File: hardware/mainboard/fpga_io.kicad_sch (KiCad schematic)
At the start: 24 parts, among them U1 LIFCL_40_CABGA400, X1 XO32

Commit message: First pass at routing done
Signed-off-by: David Shah <dave@ds0.me>
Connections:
- net +1V8: no longer C41.1, C44.1, U1.N17 (VCCIO2), U1.U19 (VCCIO2)
- net +3V3: now also C41.1, C44.1, U1.N17 (VCCIO2), U1.U19 (VCCIO2)
- net M2_DISABLE1: now also U1.W20 (PR44A/+); no longer U1.M6 (PL38A/+)
- net M2_DISABLE2: now also U1.Y19 (PR49B/-); no longer U1.M5 (PL36B/-)
- net M2_~RST: now also U1.W19 (PR49A/+); no longer U1.M4 (PL36A/+)
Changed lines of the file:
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@@
+    (stroke (width 0) (type solid) (color 0 0 0 0))
+  )
+  (wire (pts (xy 57.15 210.82) (xy 64.77 210.82))
+    (stroke (width 0) (type solid) (color 0 0 0 0))
+  )
+  (wire (pts (xy 57.15 213.36) (xy 64.77 213.36))
+    (stroke (width 0) (type solid) (color 0 0 0 0))
+  )
+  (wire (pts (xy 57.15 226.06) (xy 64.77 226.06))
     (stroke (width 0) (type solid) (color 0 0 0 0))
   )
@@
   )
   (wire (pts (xy 323.85 66.04) (xy 331.47 66.04))
-    (stroke (width 0) (type solid) (color 0 0 0 0))
-  )
-  (wire (pts (xy 323.85 76.2) (xy 331.47 76.2))
-    (stroke (width 0) (type solid) (color 0 0 0 0))
-  )
-  (wire (pts (xy 323.85 78.74) (xy 331.47 78.74))
-    (stroke (width 0) (type solid) (color 0 0 0 0))
-  )
-  (wire (pts (xy 323.85 81.28) (xy 331.47 81.28))
     (stroke (width 0) (type solid) (color 0 0 0 0))
   )
@@
     )
   )
+  (global_label "M2_~RST" (shape input) (at 57.15 210.82 180)
+    (effects (font (size 1.27 1.27)) (justify right))
+    (property "Intersheet References" "${INTERSHEET_REFS}" (id 0) (at 52.9228 210.7406 0)
+      (effects (font (size 1.27 1.27)) (justify left) hide)
+    )
+  )
+  (global_label "M2_DISABLE2" (shape input) (at 57.15 213.36 180)
+    (effects (font (size 1.27 1.27)) (justify right))
+    (property "Intersheet References" "${INTERSHEET_REFS}" (id 0) (at 58.3052 213.2806 0)
+      (effects (font (size 1.27 1.27)) (justify left) hide)
+    )
+  )
+  (global_label "M2_DISABLE1" (shape input) (at 57.15 226.06 180)
+    (effects (font (size 1.27 1.27)) (justify right))
+    (property "Intersheet References" "${INTERSHEET_REFS}" (id 0) (at 58.3052 225.9806 0)
+      (effects (font (size 1.27 1.27)) (justify left) hide)
+    )
+  )
   (global_label "B2BL_CLKI+" (shape input) (at 165.1 45.72 180)
     (effects (font (size 1.27 1.27)) (justify right))
@@
     (property "Intersheet References" "${INTERSHEET_REFS}" (id 0) (at 314.2281 65.9606 0)
       (effects (font (size 1.27 1.27)) (justify right) hide)
-    )
-  )
-  (global_label "M2_~RST" (shape input) (at 323.85 76.2 180)
-    (effects (font (size 1.27 1.27)) (justify right))
-    (property "Intersheet References" "${INTERSHEET_REFS}" (id 0) (at 319.6228 76.1206 0)
-      (effects (font (size 1.27 1.27)) (justify left) hide)
-    )
-  )
-  (global_label "M2_DISABLE2" (shape input) (at 323.85 78.74 180)
-    (effects (font (size 1.27 1.27)) (justify right))
-    (property "Intersheet References" "${INTERSHEET_REFS}" (id 0) (at 325.0052 78.6606 0)
-      (effects (font (size 1.27 1.27)) (justify left) hide)
-    )
-  )
-  (global_label "M2_DISABLE1" (shape input) (at 323.85 81.28 180)
-    (effects (font (size 1.27 1.27)) (justify right))
-    (property "Intersheet References" "${INTERSHEET_REFS}" (id 0) (at 325.0052 81.2006 0)
-      (effects (font (size 1.27 1.27)) (justify left) hide)
     )
   )
@@
     (pin "1")
   )
-  (symbol (lib_id "power:+1V8") (at 95.25 182.88 0) (unit 1)
+  (symbol (lib_id "power:+3V3") (at 95.25 182.88 0) (unit 1)
     (in_bom yes) (on_board yes)
-    (property "Reference" "#PWR032" (id 0) (at 95.25 186.69 0)
+    (property "Reference" "#PWR0114" (id 0) (at 95.25 186.69 0)
       (effects (font (size 1.27 1.27)) hide)
     )
-    (property "Value" "+1V8" (id 1) (at 95.6183 178.5556 0))
+    (property "Value" "+3V3" (id 1) (at 95.6183 178.5556 0))
     (property "Footprint" "" (id 2) (at 95.25 182.88 0)
       (effects (font (size 1.27 1.27)) hide)

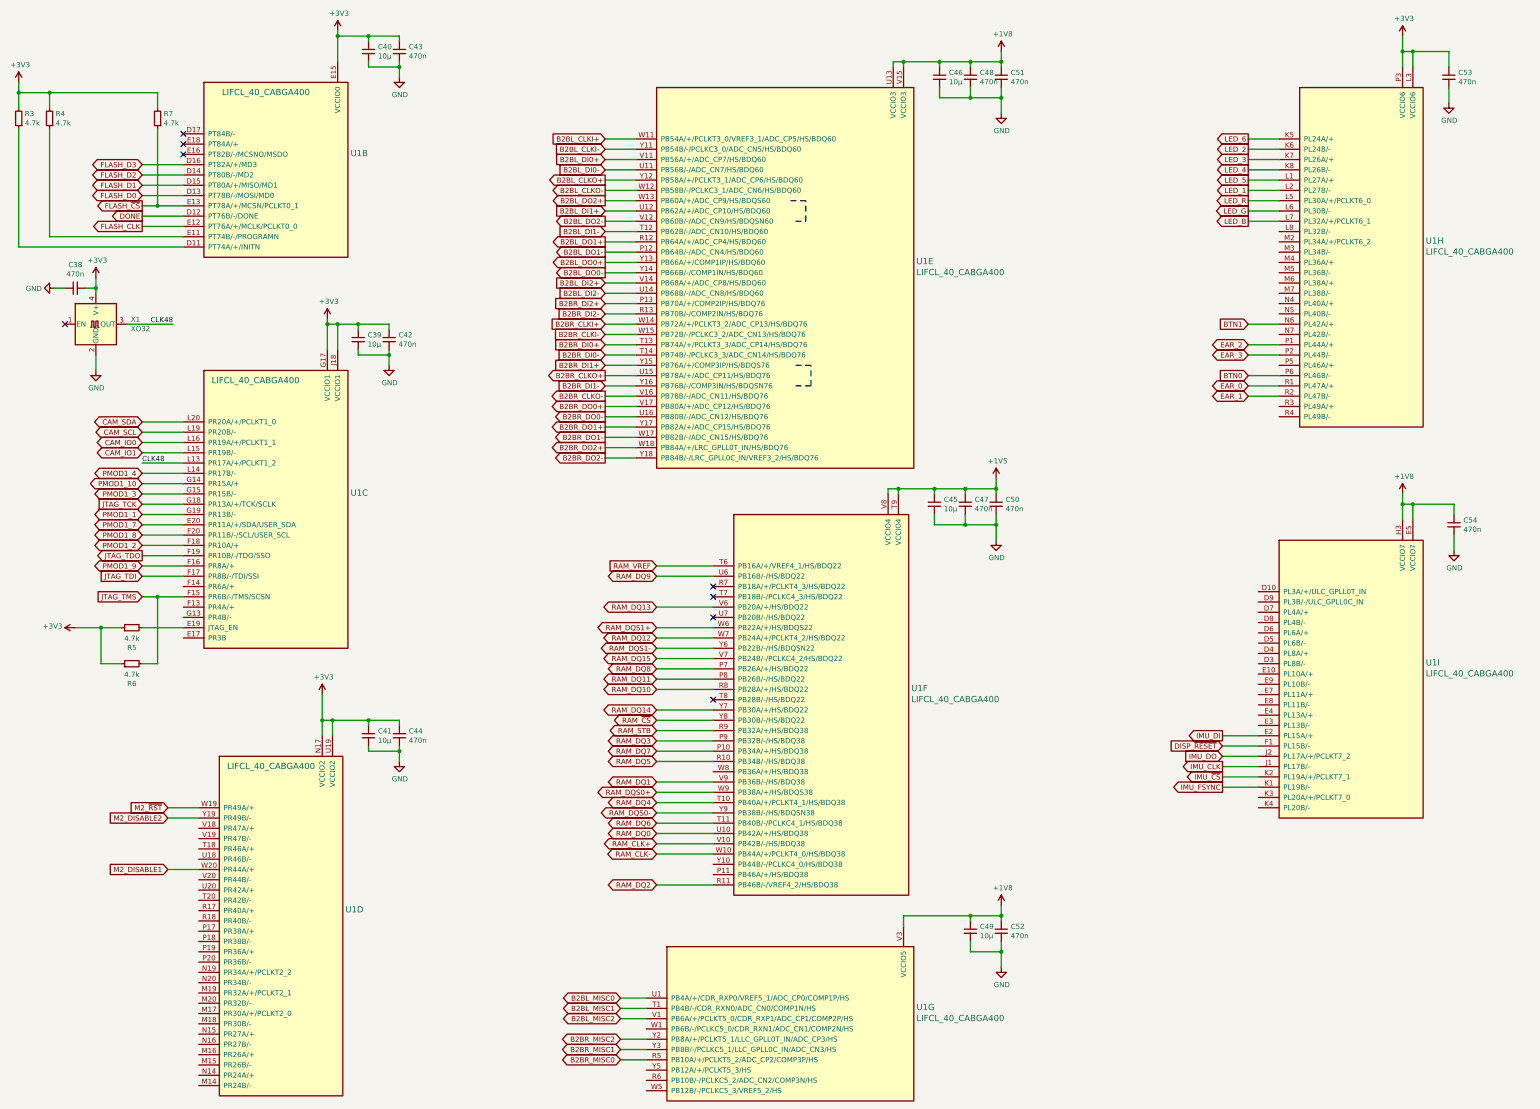
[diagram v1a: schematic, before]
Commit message: mainboard: Fix some schematic ERC issues
Signed-off-by: gatecat <gatecat@ds0.me>
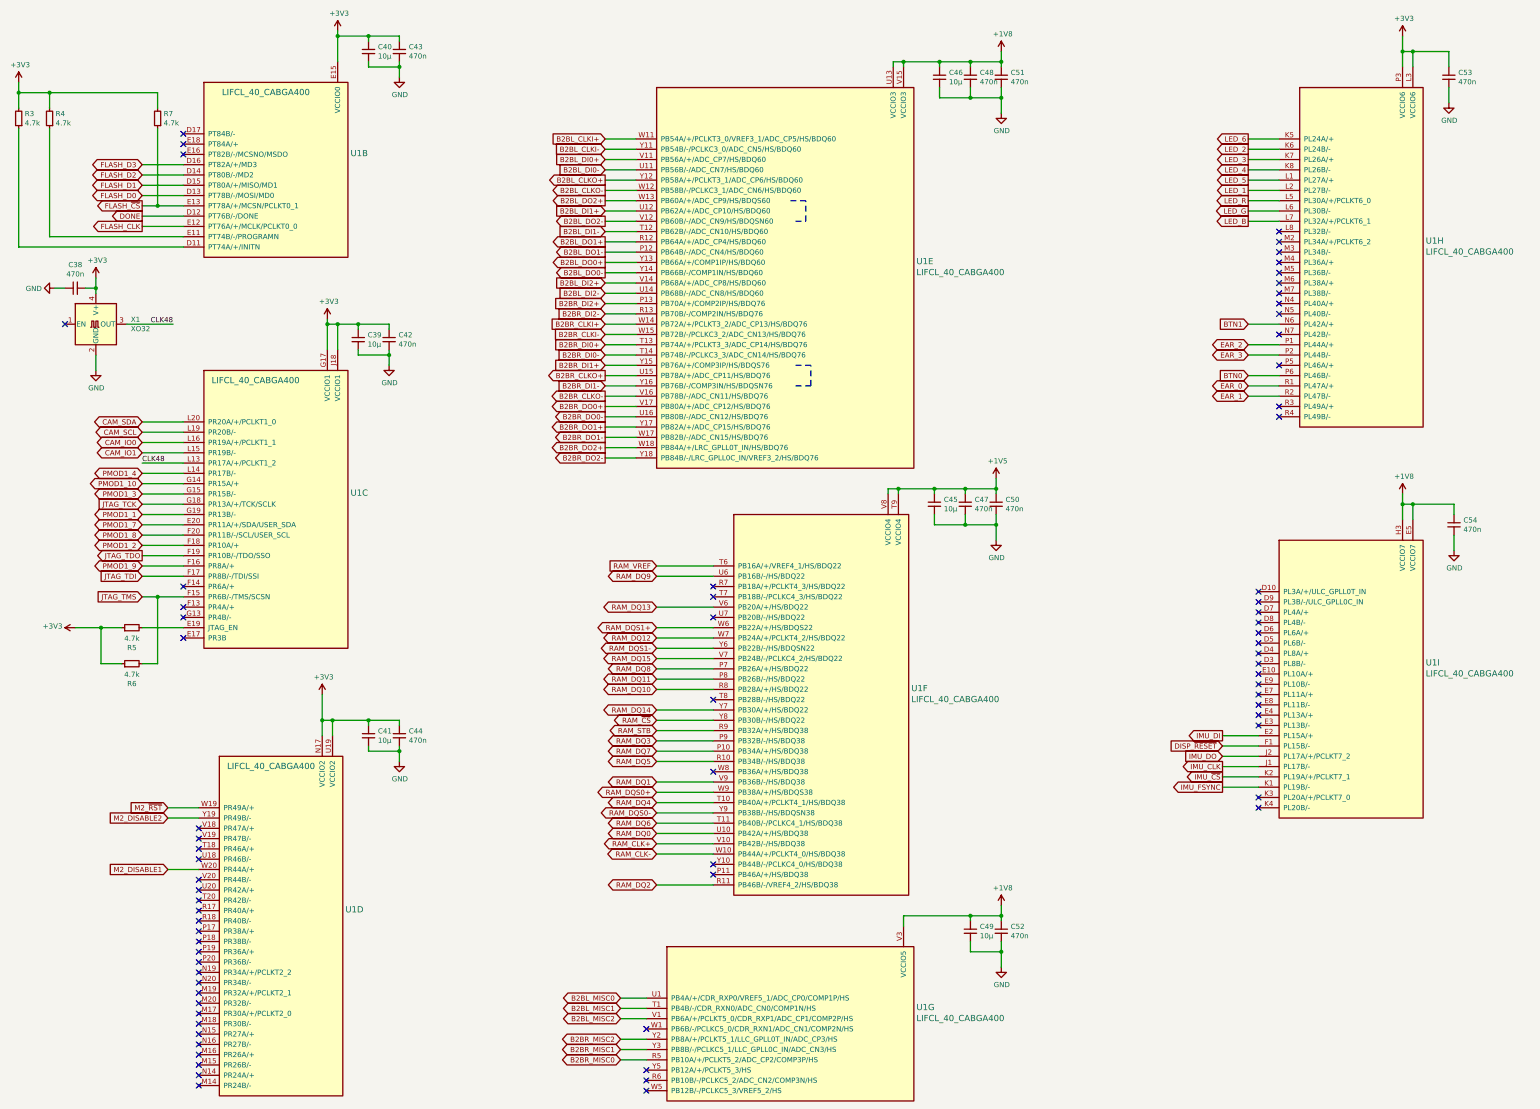
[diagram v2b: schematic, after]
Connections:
- no-connect marks 8 -> 73
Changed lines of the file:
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@@
   (no_connect (at 60.96 46.99))
   (no_connect (at 60.96 49.53))
+  (no_connect (at 60.96 156.21))
+  (no_connect (at 60.96 161.29))
+  (no_connect (at 60.96 163.83))
+  (no_connect (at 60.96 168.91))
+  (no_connect (at 64.77 215.9))
+  (no_connect (at 64.77 218.44))
+  (no_connect (at 64.77 220.98))
+  (no_connect (at 64.77 223.52))
+  (no_connect (at 64.77 228.6))
+  (no_connect (at 64.77 231.14))
+  (no_connect (at 64.77 233.68))
+  (no_connect (at 64.77 236.22))
+  (no_connect (at 64.77 238.76))
+  (no_connect (at 64.77 241.3))
+  (no_connect (at 64.77 243.84))
+  (no_connect (at 64.77 246.38))
+  (no_connect (at 64.77 248.92))
+  (no_connect (at 64.77 251.46))
+  (no_connect (at 64.77 254))
+  (no_connect (at 64.77 256.54))
+  (no_connect (at 64.77 259.08))
+  (no_connect (at 64.77 261.62))
+  (no_connect (at 64.77 264.16))
+  (no_connect (at 64.77 266.7))
+  (no_connect (at 64.77 269.24))
+  (no_connect (at 64.77 271.78))
+  (no_connect (at 64.77 274.32))
+  (no_connect (at 64.77 276.86))
+  (no_connect (at 64.77 279.4))
+  (no_connect (at 175.26 265.43))
+  (no_connect (at 175.26 275.59))
+  (no_connect (at 175.26 278.13))
+  (no_connect (at 175.26 280.67))
   (no_connect (at 191.77 156.21))
   (no_connect (at 191.77 158.75))
   (no_connect (at 191.77 163.83))
   (no_connect (at 191.77 184.15))
+  (no_connect (at 191.77 201.93))
+  (no_connect (at 191.77 224.79))
+  (no_connect (at 191.77 227.33))
+  (no_connect (at 326.39 157.48))
+  (no_connect (at 326.39 160.02))
+  (no_connect (at 326.39 162.56))
+  (no_connect (at 326.39 165.1))
+  (no_connect (at 326.39 167.64))
+  (no_connect (at 326.39 170.18))
+  (no_connect (at 326.39 172.72))
+  (no_connect (at 326.39 175.26))
+  (no_connect (at 326.39 177.8))
+  (no_connect (at 326.39 180.34))
+  (no_connect (at 326.39 182.88))
+  (no_connect (at 326.39 185.42))
+  (no_connect (at 326.39 187.96))
+  (no_connect (at 326.39 190.5))
+  (no_connect (at 326.39 208.28))
+  (no_connect (at 326.39 210.82))
+  (no_connect (at 331.47 68.58))
+  (no_connect (at 331.47 71.12))
+  (no_connect (at 331.47 73.66))
+  (no_connect (at 331.47 76.2))
+  (no_connect (at 331.47 78.74))
+  (no_connect (at 331.47 81.28))
+  (no_connect (at 331.47 83.82))
+  (no_connect (at 331.47 86.36))
+  (no_connect (at 331.47 88.9))
+  (no_connect (at 331.47 93.98))
+  (no_connect (at 331.47 101.6))
+  (no_connect (at 331.47 111.76))
+  (no_connect (at 331.47 114.3))
   (wire (pts (xy 20.32 31.75) (xy 20.32 34.29))
     (stroke (width 0) (type solid) (color 0 0 0 0))
@@
       (effects (font (size 1.524 1.524)) (justify right) hide)
     )
-    (pin "E15")
-    (pin "D17")
-    (pin "E18")
-    (pin "E16")
-    (pin "D16")
+    (pin "D11")
+    (pin "D12")
+    (pin "D13")
     (pin "D14")
     (pin "D15")
-    (pin "D13")
+    (pin "D16")
+    (pin "D17")
+    (pin "E11")
+    (pin "E12")
     (pin "E13")
-    (pin "D12")
-    (pin "E12")
-    (pin "E11")
-    (pin "D11")
+    (pin "E15")
+    (pin "E16")
+    (pin "E18")
   )
   (symbol (lib_id "meowality:LIFCL_40_CABGA400") (at 175.26 257.81 0) (unit 7)
@@
       (effects (font (size 1.524 1.524)) (justify right) hide)
     )
+    (pin "R5")
+    (pin "R6")
+    (pin "T1")
+    (pin "U1")
+    (pin "V1")
     (pin "V3")
-    (pin "U1")
-    (pin "T1")
-    (pin "V1")
     (pin "W1")
+    (pin "W5")
     (pin "Y2")
     (pin "Y3")
-    (pin "R5")
     (pin "Y5")
-    (pin "R6")
-    (pin "W5")
   )
   (symbol (lib_id "meowality:LIFCL_40_CABGA400") (at 60.96 115.57 0) (unit 3)
@@
       (effects (font (size 1.524 1.524)) (justify right) hide)
     )
+    (pin "E17")
+    (pin "E19")
+    (pin "E20")
+    (pin "F13")
+    (pin "F14")
+    (pin "F15")
+    (pin "F16")
+    (pin "F17")
+    (pin "F18")
+    (pin "F19")
+    (pin "F20")
+    (pin "G13")
+    (pin "G14")
+    (pin "G15")
+    (pin "G17")
+    (pin "G18")
+    (pin "G19")
     (pin "J18")
-    (pin "G17")
-    (pin "L20")
-    (pin "L19")
-    (pin "L16")
-    (pin "L15")
     (pin "L13")
     (pin "L14")
-    (pin "G14")
-    (pin "G15")
-    (pin "G18")
-    (pin "G19")
-    (pin "E20")
-    (pin "F20")
-    (pin "F18")
-    (pin "F19")
-    (pin "F16")
-    (pin "F17")
-    (pin "F14")
-    (pin "F15")
-    (pin "F13")
-    (pin "G13")
-    (pin "E19")
-    (pin "E17")
+    (pin "L15")
+    (pin "L16")
+    (pin "L19")
+    (pin "L20")
   )
   (symbol (lib_id "meowality:LIFCL_40_CABGA400") (at 326.39 157.48 0) (unit 9)
@@
       (effects (font (size 1.524 1.524)) (justify right) hide)
     )
-    (pin "E5")
-    (pin "H3")
     (pin "D10")
-    (pin "D9")
+    (pin "D3")
+    (pin "D4")
+    (pin "D5")
+    (pin "D6")
     (pin "D7")
     (pin "D8")
-    (pin "D6")
-    (pin "D5")
-    (pin "D4")
-    (pin "D3")
+    (pin "D9")
     (pin "E10")
-    (pin "E9")
+    (pin "E2")
+    (pin "E3")
+    (pin "E4")
+    (pin "E5")
     (pin "E7")
     (pin "E8")
-    (pin "E4")
-    (pin "E3")
-    (pin "E2")
+    (pin "E9")
     (pin "F1")
+    (pin "H3")
+    (pin "J1")
     (pin "J2")
-    (pin "J1")
+    (pin "K1")
     (pin "K2")
-    (pin "K1")
     (pin "K3")
     (pin "K4")
@@
       (effects (font (size 1.524 1.524)) (justify right) hide)
     )
-    (pin "U19")
+    (pin "M14")
+    (pin "M15")
+    (pin "M16")
+    (pin "M17")
+    (pin "M18")
+    (pin "M19")
+    (pin "M20")
+    (pin "N14")
+    (pin "N15")
+    (pin "N16")
     (pin "N17")
-    (pin "W19")
-    (pin "Y19")
-    (pin "V18")
-    (pin "V19")
-    (pin "T18")
-    (pin "U18")
-    (pin "W20")
-    (pin "V20")
-    (pin "U20")
-    (pin "T20")
-    (pin "R17")
-    (pin "R18")
+    (pin "N19")
+    (pin "N20")
     (pin "P17")
     (pin "P18")
     (pin "P19")
     (pin "P20")
-    (pin "N19")
-    (pin "N20")
-    (pin "M19")
-    (pin "M20")
-    (pin "M17")
-    (pin "M18")
-    (pin "N15")
-    (pin "N16")
-    (pin "M16")
-    (pin "M15")
-    (pin "N14")
-    (pin "M14")
+    (pin "R17")
+    (pin "R18")
+    (pin "T18")
+    (pin "T20")
+    (pin "U18")
+    (pin "U19")
+    (pin "U20")
+    (pin "V18")
+    (pin "V19")
+    (pin "V20")
+    (pin "W19")
+    (pin "W20")
+    (pin "Y19")
   )
   (symbol (lib_id "meowality:LIFCL_40_CABGA400") (at 331.47 45.72 0) (unit 8)
@@
       (effects (font (size 1.524 1.524)) (justify right) hide)
     )
-    (pin "L3")
-    (pin "P3")
     (pin "K5")
     (pin "K6")
@@
     (pin "L1")
     (pin "L2")
+    (pin "L3")
     (pin "L5")
     (pin "L6")
@@
     (pin "P1")
     (pin "P2")
+    (pin "P3")
     (pin "P5")
     (pin "P6")
@@
       (effects (font (size 1.524 1.524)) (justify right) hide)
     )
+    (pin "P10")
+    (pin "P11")
+    (pin "P7")
+    (pin "P8")
+    (pin "P9")
+    (pin "R10")
+    (pin "R11")
+    (pin "R7")
+    (pin "R8")
+    (pin "R9")
+    (pin "T10")
+    (pin "T11")
+    (pin "T6")
+    (pin "T7")
+    (pin "T8")
     (pin "T9")
+    (pin "U10")
+    (pin "U6")
+    (pin "U7")
+    (pin "V10")
+    (pin "V6")
+    (pin "V7")
     (pin "V8")
-    (pin "T6")
-    (pin "U6")
-    (pin "R7")
-    (pin "T7")
-    (pin "V6")
-    (pin "U7")
+    (pin "V9")
+    (pin "W10")
     (pin "W6")
     (pin "W7")
+    (pin "W8")
+    (pin "W9")
+    (pin "Y10")
     (pin "Y6")
-    (pin "V7")
-    (pin "P7")
-    (pin "P8")
-    (pin "R8")
-    (pin "T8")
     (pin "Y7")
     (pin "Y8")
-    (pin "R9")
-    (pin "P9")
-    (pin "P10")
-    (pin "R10")
-    (pin "W8")
-    (pin "V9")
-    (pin "W9")
-    (pin "T10")
     (pin "Y9")
-    (pin "T11")
-    (pin "U10")
-    (pin "V10")
-    (pin "W10")
-    (pin "Y10")
-    (pin "P11")
-    (pin "R11")
   )
   (symbol (lib_id "meowality:LIFCL_40_CABGA400") (at 172.72 45.72 0) (unit 5)
@@
       (effects (font (size 1.524 1.524)) (justify right) hide)
     )
+    (pin "P12")
+    (pin "P13")
+    (pin "R12")
+    (pin "R13")
+    (pin "T12")
+    (pin "T13")
+    (pin "T14")
+    (pin "U11")
+    (pin "U12")
+    (pin "U13")
+    (pin "U14")
+    (pin "U15")
+    (pin "U16")
+    (pin "V11")
+    (pin "V12")
+    (pin "V14")
     (pin "V15")
-    (pin "U13")
+    (pin "V16")
+    (pin "V17")
     (pin "W11")
-    (pin "Y11")
-    (pin "V11")
-    (pin "U11")
-    (pin "Y12")
     (pin "W12")
     (pin "W13")
-    (pin "U12")
-    (pin "V12")
-    (pin "T12")
-    (pin "R12")
-    (pin "P12")
+    (pin "W14")
+    (pin "W15")
+    (pin "W17")
+    (pin "W18")
+    (pin "Y11")
+    (pin "Y12")
     (pin "Y13")
     (pin "Y14")
-    (pin "V14")
-    (pin "U14")
-    (pin "P13")
-    (pin "R13")
-    (pin "W14")
-    (pin "W15")
-    (pin "T13")
-    (pin "T14")
     (pin "Y15")
-    (pin "U15")
     (pin "Y16")
-    (pin "V16")
-    (pin "V17")
-    (pin "U16")
     (pin "Y17")
-    (pin "W17")
-    (pin "W18")
     (pin "Y18")
   )
